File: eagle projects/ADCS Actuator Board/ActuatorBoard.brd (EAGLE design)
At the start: 91 x 91 mm, 155 parts, among them J19 TE_1-84953-1, J20 TE_1-84953-1, J21 TE_1-84953-1, J7 CNC_3221-10-0300-00, J8 CNC_3221-14-0300-00, U1 TVS991, U10 DRV10970_MOTOR_DRIVERDRV10970, U12 DRV10970_MOTOR_DRIVERDRV10970, U2 ADS7841E_2K5, U3 ADS7841E_2K5, U35 BD6210F-E2, U39 BD6210F-E2, U5 TVS991, U7 DRV10970_MOTOR_DRIVERDRV10970, U8 TVS991, U9 BD6210F-E2

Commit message: Staring REV B Act board
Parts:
- removed C119, C121, C122, C126, C129, C130, C139, C142, C25, C26: 0.1u, rcl:C0603
- removed C120, C140: 1u, rcl:C0603
- removed C123, C131: 0.1u, rcl:C0402
- removed C125, C141: 0.33u, rcl:C0603
- removed C127, C143: 2.2u, rcl:C0603
- removed C128, C144: 10u, rcl:C0603
- removed J19, J20, J21: TE_1-84953-1, my_library:TE_1-84953-1
- removed J5: (no value), my_library:1X03
- removed JP7, JP9: (no value), my_library:1X02
- removed JX, JY, JZ: (no value), my_library:2POL254
- removed R23: 100R, rcl:M0805
- removed R28, R29, R37, R38, R5: 1.8k, rcl:R0402
- removed R3, R4, R76: 5.1k, rcl:R0402
- removed R73, R74: 3.3k, rcl:R0603
- removed TP35, TP36, TP43, TP44, TP46, TP54, TP7: TESTPOINT, my_library:TP_P76H50
- removed U1: TVS991, my_library:SOT95P280X145-5N
- removed U35, U39, U9: BD6210F-E2, my_library:BD6221F-E2_SOIC8P127_500X620X171L30X42N
- added C1, C11, C2, C20, C34, C45, C50, C51, C54, C58, C63: 0.1u, rcl:C0603
- added C10, C3, C4, C46, C52, C6, C8: 0.1u, rcl:C0402
- added C12, C32, C55, C62: 1u, rcl:C0603
- added C19, C57: 0.33u, rcl:C0603
- added C28, C35, C59: 2.2u, rcl:C0603
- added C30, C36, C60: 10u, rcl:C0603
- added C31, C38, C61: 0.01u, rcl:C0603
- added C5, C7, C9: 1u, rcl:C0402
- added J11, J2: TE_1-84953-1, my_library:TE_1-84953-1
- added J12, J3: (no value), my_library:1X03
- added JP2, JP3: (no value), pinhead:1X02
- added R102, R103, R59, R60: 10K, rcl:R0603
- added R104, R61: 75K, rcl:R0603
- added R105, R106, R62, R63: 3.3k, rcl:R0603
- added R107, R108, R109, R64, R65, R66: 4.7k, rcl:R0402
- added R110, R111, R112, R113, R114, R115, R58, R67, R68, R69, R70, R71, R75: 5.1M, rcl:R0402
- added R116, R77: 10k, rcl:R0603
- added R117, R78: 2k, rcl:R0603
- added R118, R79: 1k, rcl:R0603
- added R119, R80: 100k, rcl:R0603
- added R47, R89: 0R, rcl:M0805
- added R57: 10K, rcl:R0402
- added R81: 5.1k, rcl:R0402
- added R82: 100R, rcl:M0805
- added R88: DNP, rcl:M0805
- added TP1, TP10, TP11, TP12, TP13, TP14, TP15, TP16, TP17, TP18, TP19, TP20, TP26, TP27, TP28, TP29, TP33, TP37, TP38, TP39, TP47, TP48, TP49, TP50, TP53, TP55, TP56, TP57, TP58, TP59, TP60, TP61, TP62, TP63, TP8, TP9: TESTPOINT, my_library:TP_P76H50
- added U11, U18: BD6210F-E2, my_library:BD6221F-E2_SOIC8P127_500X620X171L30X42N
- added U13, U17: LM2917MX/NOPB, my_library:SOIC14P127_865X600X175L83X41N_LM2917MX-NOPB
- added U16, U6: DRV10970_MOTOR_DRIVERDRV10970, my_library:SOP65P640X120-25T240X328N
- added U19: TSV991AILT, my_library:SOT95P280X145-5N
- added U4: ADS7841E_2K5, my_library:DBQ16
- C27: device rcl:C0402 -> rcl:C0603
- C41: value 2.2u -> 1u
- C42: value 10u -> 0.1u
- J4: value (none) -> TE_1-84953-1; device my_library:1X03 -> my_library:TE_1-84953-1
- JP5: device my_library:1X02 -> pinhead:1X02
- R1, R2: value 4.7k -> 10K; device rcl:R0402 -> rcl:R0603
- R11: value 4.7k -> 100R; device rcl:R0402 -> rcl:M0805
- R12: value 4.7k -> 5.1k
- R15: value 4.7k -> 1.8k
- R16: value 100R -> 1.8k; device rcl:M0805 -> rcl:R0402
- R17: value 5.1k -> 1.8k
- R19, R20: value 10K -> 4.7k; device rcl:R0603 -> rcl:R0402
- R21: value 75K -> 5.1M; device rcl:R0603 -> rcl:R0402
- R22: value 100R -> DNP
- R24: value 1.8k -> 0R; device rcl:R0402 -> rcl:M0805
- R25, R31: value 1.8k -> 5.1k
- R30: value 5.1k -> 100R; device rcl:R0402 -> rcl:M0805
- R35, R36: value 3.3k -> 5.1M; device rcl:R0603 -> rcl:R0402
- R41: value 5.1M -> 1.8k
- R42: value 5.1M -> DNP; device rcl:R0402 -> rcl:M0805
- R44: value 5.1M -> 10k; device rcl:R0402 -> rcl:R0603
- R48: value 10K -> 2k
- R49: value 10K -> 1k
- R7: value 4.7k -> 75K; device rcl:R0402 -> rcl:R0603
- R72: value 75K -> 100k
- R8, R9: value 4.7k -> 3.3k; device rcl:R0402 -> rcl:R0603
- R83: value 10K -> 5.1k; device rcl:R0603 -> rcl:R0402
- R84: value 10K -> 1.8k; device rcl:R0603 -> rcl:R0402
- R85: value 75K -> 1.8k; device rcl:R0603 -> rcl:R0402
- R86, R87: value 3.3k -> 1.8k; device rcl:R0603 -> rcl:R0402
- U10: value DRV10970_MOTOR_DRIVERDRV10970 -> LM2917MX/NOPB; device my_library:SOP65P640X120-25T240X328N -> my_library:SOIC14P127_865X600X175L83X41N_LM2917MX-NOPB
- U12: value DRV10970_MOTOR_DRIVERDRV10970 -> TSV991AILT; device my_library:SOP65P640X120-25T240X328N -> my_library:SOT95P280X145-5N
- U5: value TVS991 -> BD6210F-E2; device my_library:SOT95P280X145-5N -> my_library:BD6221F-E2_SOIC8P127_500X620X171L30X42N
- U8: value TVS991 -> TSV991AILT
- moved R45 169.7 mm to (107.3, 94.0)
- moved R46 169.7 mm to (112.4, 94.0)
- moved R41 158.8 mm to (11.4, 67.9), flipped to the bottom, turned to 270 degrees
- moved R42 151.7 mm to (18.4, 61.0), flipped to the bottom
- moved R34 149.3 mm to (12.7, 67.9), flipped to the bottom
- moved R44 145.8 mm to (34.3, 57.1), turned to 0 degrees
- moved R32 145.0 mm to (11.4, 65.7), flipped to the bottom, turned to 270 degrees
- moved R33 141.3 mm to (11.4, 60.6), flipped to the bottom, turned to 270 degrees
- moved R31 140.7 mm to (12.1, 62.5), flipped to the bottom, turned to 180 degrees
- moved R25 139.9 mm to (12.1, 63.8), flipped to the bottom, turned to 180 degrees
- moved R43 136.8 mm to (41.3, 52.4), flipped to the bottom, turned to 270 degrees
- moved R40 131.8 mm to (42.5, 52.4), flipped to the bottom, turned to 270 degrees
- moved R39 131.5 mm to (38.7, 52.4), flipped to the bottom, turned to 270 degrees
- moved R6 129.6 mm to (12.1, 51.1), flipped to the bottom, turned to 180 degrees
- moved R24 128.3 mm to (18.4, 52.7), flipped to the bottom
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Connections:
- removed net MAG_CUR_SEN_Y: R22.2, R30.2, U35.1
- removed net MAG_CUR_SEN_Z: R16.2, R17.2, U39.1
- removed net MAG_Y_FIN: TP43.1, U35.4
- removed net N$10: R28.2, R76.1, U1.3
- removed net N$105: C139.1, U12.9
- removed net N$106: C140.2, U12.8
- removed net N$107: C139.2, U12.10
- removed net N$108: C143.1, U12.16
- removed net N$109: C141.1, U12.22
- removed net N$18: R28.1, R37.1, R38.2
- removed net N$19 (its old number): R40.2, U10.1
- removed net N$23 (its old number): R43.1, U10.20
- removed net N$3 (its old number): R39.2, U7.1
- removed net N$33: JP7.2, U35.7
- removed net N$4: R5.1, R6.1, U8.4
- removed net N$67: JP9.2, U39.7
- removed net N$7: R29.1, R4.1, U1.4
- removed net N$87: C119.1, U10.9
- removed net N$88: C120.2, U10.8
- removed net N$89: C119.2, U10.10
- removed net N$90: C127.1, U10.16
- removed net N$91: C125.1, U10.22
- removed net OUT1_Y: JY.1, R22.1, R3.2
- removed net OUT1_Z: JZ.1, R16.1, R23.1, R4.2, R6.2
- removed net OUT2_Y: JP7.1, JY.2
- removed net OUT2_Z: JP9.1, JZ.2
- new net !CS!_SPD_SENSE_RW: J7.1, U4.15
- new net N$28: R21.2, U7.1
- new net N$29: R35.1, U7.20
- new net N$30: C41.2, R72.2, TP13.1, U10.3, U10.4
- new net N$31: R48.1, R49.2, U10.11
- new net N$32: C8.1, R57.1, U4.7
- new net N$34: TP1.1, U4.5
- new net N$35: R58.2, U4.13
- new net N$36: C11.1, U6.9
- new net N$38: C12.2, U6.8
- new net N$39: C11.2, U6.10
- new net N$40: C28.1, U6.16
- new net N$41: C19.1, U6.22
- new net N$43: R67.2, U6.1
- new net N$44: R68.1, U6.20
- new net N$49: C32.2, R80.2, TP28.1, U13.3, U13.4
- new net N$50: R78.1, R79.2, U13.11
- new net N$51: C31.2, U13.2
- new net N$52: C38.2, U10.2
- new net N$53: R81.1, R84.2, U19.3
- new net N$54: R84.1, R86.1, R87.2
- new net N$55: R82.2, R88.2, R89.1
- new net N$63: C54.1, U16.9
- new net N$64: C55.2, U16.8
- new net N$65: C54.2, U16.10
- new net N$66: C59.1, U16.16
- new net N$68: C57.1, U16.22
- new net N$69: R110.2, U16.1
- new net N$70: R111.1, U16.20
- new net N$72: R117.1, R118.2, U17.11
- new net N$73: C61.2, U17.2
- new net RW_X_SPD: R44.2, TP12.1, U10.10, U10.5, U4.3
- new net RW_Y_SPD: R116.2, TP56.1, U17.10, U17.5, U4.2
- new net RW_Z_SPD: R77.2, TP27.1, U13.10, U13.5, U4.4
- new net X_DNC_1: R36.1, U10.6
- new net X_DNC_2: R39.1, U10.7
- new net X_DNC_3: R43.1, U10.14
- new net X_DNC_4: R40.1, U10.13
- new net Y_DNC_1: R112.1, U17.6
- new net Y_DNC_2: R113.1, U17.7
- new net Y_DNC_3: R115.1, U17.14
- new net Y_DNC_4: R114.1, U17.13
- new net Z_DNC_1: R69.1, U13.6
- new net Z_DNC_2: R70.1, U13.7
- new net Z_DNC_3: R75.1, U13.14
- new net Z_DNC_4: R71.1, U13.13
- net +3V3: now also C10.1, C34.2, C4.1, C42.2, C5.1, C6.1, C63.2, C7.1, C9.1, R105.1, R106.1, R118.1, R17.2, R34.2, R49.1, R57.2, R62.1, R63.1, R79.1, R8.1, R86.2, R9.1, U10.8, U10.9, U13.8, U13.9, U17.8, U17.9, U4.1, U4.8, U4.9; no longer R31.2, R33.2, R35.1, R36.1, R37.2, R73.1, R74.1, R86.1, R87.1
- net +5V: now also C1.1, C12.1, C2.2, C3.1, C30.1, C36.1, C45.2, C46.1, C50.1, C51.2, C52.1, C55.1, C60.1, J11.1, J12.3, J2.1, J3.3, J4.1, R102.2, R107.2, R108.2, R109.2, R20.2, R59.2, R64.2, R65.2, R66.2, U11.2, U11.3, U11.6, U12.5, U16.15, U18.2, U18.3, U18.6, U19.5, U5.2, U5.3, U5.6, U6.15; no longer C120.1, C121.1, C122.2, C123.1, C128.1, C129.1, C130.2, C131.1, C140.1, C144.1, C25.1, C26.2, C42.1, J19.1, J20.1, J21.1, J4.3, J5.3, R11.2, R12.2, R15.2, R2.2, R48.2, R7.2, R8.2, R83.2, R9.2, U1.5, U10.15, U12.15, U35.2, U35.3, U35.6, U39.2, U39.3, U39.6, U5.5, U9.2, U9.3, U9.6
- net BRKMOD_X: now also J6.2, U7.21; no longer J4.2, U10.21
- net BRKMOD_Y: now also J12.2, U16.21; no longer J6.2, U7.21
- net BRKMOD_Z: now also J3.2, U6.21; no longer J5.2, U12.21
- net CUR_OUT1: no longer R5.2, U8.1
- net CUR_OUT2: no longer R24.2, TP46.1, U5.1
- net CUR_OUT3: now also R16.2, R33.2, R85.2, TP10.1, TP30.1, TP51.1, U12.1, U19.1, U8.1; no longer R29.2, TP54.1, U1.1
- net GND: now also C1.2, C10.2, C19.2, C2.1, C20.2, C28.2, C3.2, C30.2, C31.1, C32.1, C34.1, C35.2, C36.2, C38.1, C4.2, C41.1, C42.1, C45.1, C46.2, C5.2, C50.2, C51.1, C52.2, C57.2, C58.2, C59.2, C6.2, C60.2, C61.1, C62.1, C63.1, C7.2, C8.2, C9.2, J11.5, J11.TAB1, J11.TAB2, J12.1, J2.5, J2.TAB1, J2.TAB2, J3.1, J4.5, J4.TAB1, J4.TAB2, R103.1, R104.1, R110.1, R111.2, R112.2, R113.2, R114.2, R115.2, R116.1, R117.2, R119.1, R18.1, R2.1, R35.2, R36.2, R39.2, R40.2, R44.1, R48.2, R58.1, R60.1, R61.1, R67.1, R68.2, R69.2, R7.1, R70.2, R71.2, R75.2, R77.1, R78.2, R80.1, R87.1, U11.8, U12.2, U13.12, U16.12, U16.25, U17.12, U18.8, U19.2, U4.10, U4.11, U4.6, U5.8, U6.12, U6.25; no longer C121.2, C122.1, C123.2, C125.2, C126.2, C127.2, C128.2, C129.2, C130.1, C131.2, C141.2, C142.2, C143.2, C144.2, C25.2, C26.1, C41.2, C42.2, J19.5, J19.TAB1, J19.TAB2, J20.5, J20.TAB1, J20.TAB2, J21.5, J21.TAB1, J21.TAB2, J4.1, J5.1, R20.1, R32.1, R34.1, R38.1, R39.1, R40.1, R42.2, R44.2, R49.1, R84.1, R85.1, U1.2, U10.25, U12.12, U12.25, U35.8, U39.8, U5.2, U9.8
- net MAG_CUR_SEN_X: now also R24.2, R25.2, R47.2, R6.2, R81.2, R89.2, TP17.1, TP34.1, TP52.1, U11.1, U18.1, U5.1; no longer R23.2, R76.2, U9.1
- net MAG_X_FIN: now also TP24.1, TP47.1, TP8.1, U11.4, U18.4, U5.4; no longer TP35.1, U9.4
- net MAG_X_RIN: now also TP25.1, TP48.1, TP9.1, U11.5, U18.5, U5.5; no longer TP36.1, U9.5
- net MAG_Y_RIN: no longer TP44.1, U35.5
- net MAG_Z_FIN: no longer TP51.1, U39.4
- net MAG_Z_RIN: no longer TP52.1, U39.5
- net N$16: now also R11.2, R22.2, R24.1; no longer JP5.2, U9.7
- net N$17: now also R31.1, U12.4; no longer R34.2
- net N$20: now also R25.1, R32.2, U12.3; no longer R41.2, U12.1
- net N$21: now also R32.1, R34.1, R41.2; no longer R18.1, R31.1, R32.2
- net N$22: now also R30.2, R42.2, R47.1; no longer R42.1, U12.20
- net N$24: now also C35.1, U7.16; no longer R44.1, U7.20
- net N$48: now also R83.1, R85.1, U19.4; no longer R25.1
- net N$6: now also R12.1, R16.1, U8.4; no longer R24.1, R3.1, U5.4
- net N$71: now also C62.2, R119.2, TP57.1, U17.3, U17.4; no longer C41.1, U7.16
- net N$8: now also R15.2, R6.1; no longer R17.1, R18.2
- net N$9: now also R15.1, R17.1, R18.2; no longer R25.2, R30.1, U5.3
- net OUT1_X: now also JP2.1, JP3.1, JP5.1, R11.1, R12.2, R22.1, R30.1, R31.2, R42.1, R82.1, R83.2, R88.1, TP21.1, TP39.1, TP62.1; no longer JX.1
- net OUT2_X: now also JP2.2, JP3.2, JP5.2, TP22.1, TP40.1, TP63.1, U11.7, U18.7, U5.7; no longer JP5.1, JX.2
- net RW_X_DIR: now also U7.23; no longer U10.23
- net RW_X_I_SENS: now also R7.2, TP11.1, U7.17; no longer R72.2, TP34.1, U10.17
- net RW_X_LOCK: now also R9.2, U7.18; no longer R74.2, U10.18
- net RW_X_OUTFG: now also R8.2, TP23.1, U10.1, U7.24; no longer J8.13, R73.2, U10.24
- net RW_X_SPEED_CTRL: now also U7.19; no longer U10.19
- net RW_Y_DIR: now also U16.23; no longer U7.23
- net RW_Y_I_SENS: now also R104.2, TP55.1, U16.17; no longer R21.2, TP30.1, U7.17
- net RW_Y_LOCK: now also R106.2, U16.18; no longer R36.2, U7.18
- net RW_Y_OUTFG: now also R105.2, TP61.1, U16.24, U17.1; no longer J7.1, R35.2, U7.24
- net RW_Y_SPEED_CTRL: now also U16.19; no longer U7.19
- net RW_Z_DIR: now also U6.23; no longer U12.23
- net RW_Z_I_SENS: now also R61.2, TP26.1, U6.17; no longer R85.2, TP40.1, U12.17
- net RW_Z_LOCK: now also R63.2, U6.18; no longer R87.2, U12.18
- net RW_Z_OUTFG: now also R62.2, TP38.1, U13.1, U6.24; no longer J7.2, R86.2, U12.24
- net RW_Z_SPEED_CTRL: now also U6.19; no longer U12.19
- net UCB0_SPI_CLK: now also U4.16
- net UCB0_SPI_MISO: now also U4.12
- net UCB0_SPI_MOSI: now also U4.14
- net VINT/2_X: now also C16.1, R1.1, R2.2, U7.3, U7.5, U7.7; no longer C126.1, R48.1, R49.2, U10.3, U10.5, U10.7
- net VINT/2_Y: now also C58.1, R102.1, R103.2, U16.3, U16.5, U16.7; no longer C16.1, R19.1, R20.2, U7.3, U7.5, U7.7
- net VINT/2_Z: now also C20.1, R59.1, R60.2, U6.3, U6.5, U6.7; no longer C142.1, R83.1, R84.2, U12.3, U12.5, U12.7
- net X_HALL_A: now also J4.3, R19.1, U7.2; no longer J19.3, R2.1, U10.2
- net X_HALL_B: now also J4.4, R10.1, U7.4; no longer J19.4, R1.1, U10.4
- net X_HALL_C: now also J4.2, R20.1, U7.6; no longer J19.2, R7.1, U10.6
- net X_PHASE_A: now also J4.10, J4.11, TP14.1, U7.14; no longer J19.10, J19.11, U10.14
- net X_PHASE_B: now also J4.8, J4.9, TP15.1, U7.13; no longer J19.8, J19.9, U10.13
- net X_PHASE_C: now also U7.11; no longer J19.6, J19.7, U10.11
- net Y_HALL_A: now also J11.3, R108.1, TP53.1, U16.2; no longer J20.3, R9.1, TP25.1, U7.2
- net Y_HALL_B: now also J11.4, R107.1, TP50.1, U16.4; no longer J20.4, R8.1, TP24.1, U7.4
- net Y_HALL_C: now also J11.2, R109.1, TP49.1, U16.6; no longer J20.2, R10.1, TP23.1, U7.6
- net Y_PHASE_A: now also J11.10, J11.11, TP58.1, U16.14; no longer J20.10, J20.11, U7.14
- net Y_PHASE_B: now also J11.8, J11.9, TP59.1, U16.13; no longer J20.8, J20.9, U7.13
- net Y_PHASE_C: now also J11.6, J11.7, TP60.1, U16.11; no longer J20.6, J20.7, U7.11
- net Z_HALL_A: now also J2.3, R65.1, TP20.1, U6.2; no longer J21.3, R12.1, TP22.1, U12.2
- net Z_HALL_B: now also J2.4, R64.1, TP19.1, U6.4; no longer J21.4, R11.1, TP21.1, U12.4
- net Z_HALL_C: now also J2.2, R66.1, TP18.1, U6.6; no longer J21.2, R15.1, TP7.1, U12.6
- net Z_PHASE_A: now also J2.10, J2.11, TP29.1, U6.14; no longer J21.10, J21.11, U12.14
- net Z_PHASE_B: now also J2.8, J2.9, TP33.1, U6.13; no longer J21.8, J21.9, U12.13
- net Z_PHASE_C: now also J2.6, J2.7, J4.6, J4.7, TP16.1, TP37.1, U6.11; no longer J21.6, J21.7, U12.11
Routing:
- net RW_Y_SPEED_CTRL: track 105.1 -> 7.73 mm, vias 5 -> 0
- net RW_X_DIR: track 91.8 -> 5.49 mm, vias 5 -> 1
- net MAG_Z_RIN: track 84.2 -> 0.00 mm
- net RW_Y_OUTFG: track 100.9 -> 17.1 mm
- net MAG_Y_RIN: track 79.2 -> 0.00 mm
- net MAG_Z_FIN: track 78.1 -> 0.00 mm, vias 1 -> 0
- net RW_Y_DIR: track 82.8 -> 5.49 mm, vias 4 -> 1
- net RW_X_SPEED_CTRL: track 84.5 -> 7.73 mm, vias 3 -> 0
- net RW_X_OUTFG: track 93.6 -> 19.4 mm
- net MAG_X_RIN: track 76.1 -> 5.77 mm, vias 1 -> 0
- net MAG_X_FIN: track 69.1 -> 5.77 mm
- net !CS!_CURR_SENSE_MTQR: track 61.2 -> 0.00 mm, vias 1 -> 0
- net UCB0_SPI_CLK: track 61.1 -> 0.00 mm, vias 2 -> 0
- net UCB0_SPI_MISO: track 56.6 -> 0.00 mm, vias 1 -> 0
- net !CS!_CURR_SENSE_RW: track 50.0 -> 0.00 mm, vias 3 -> 0
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- removed copper zone on layer 15, net +5V
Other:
- board text added: "ACTUATOR BOARD - REV B"
- board text removed: "ACTUATOR BOARD - REV A"

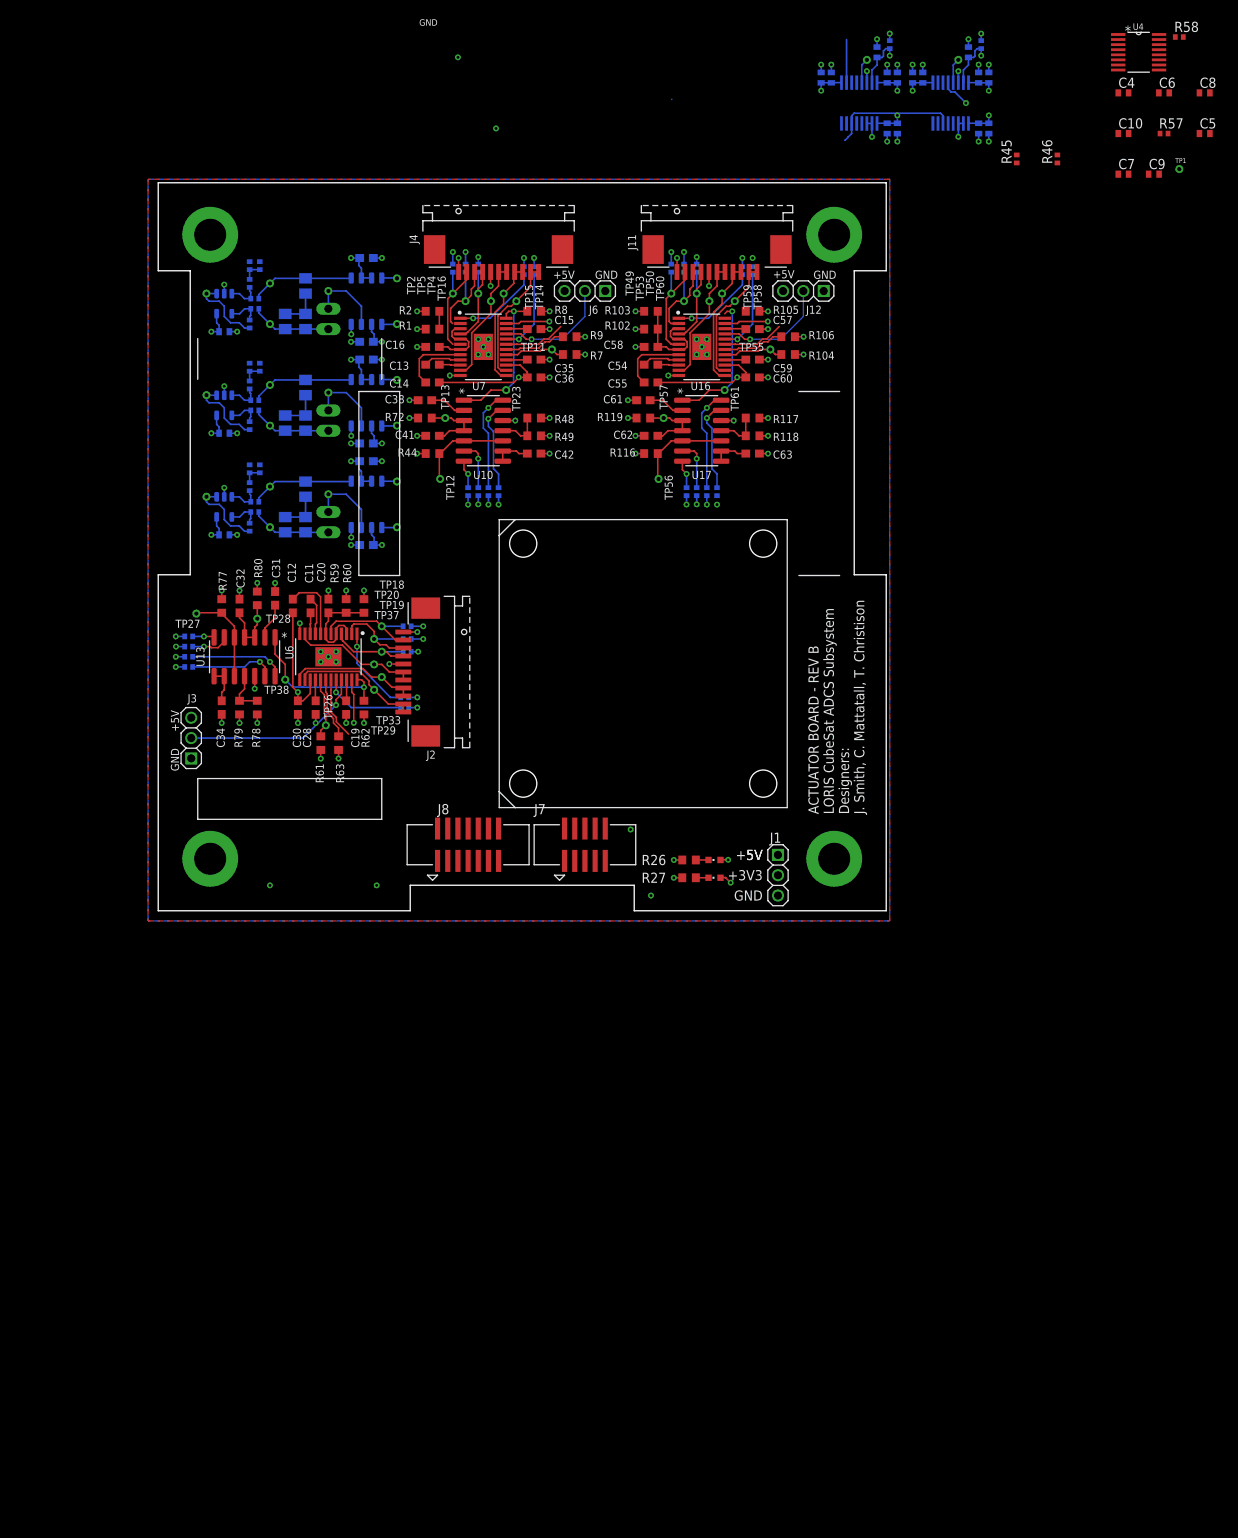
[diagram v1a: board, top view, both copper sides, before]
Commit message: Added FV converters, replaced connectors
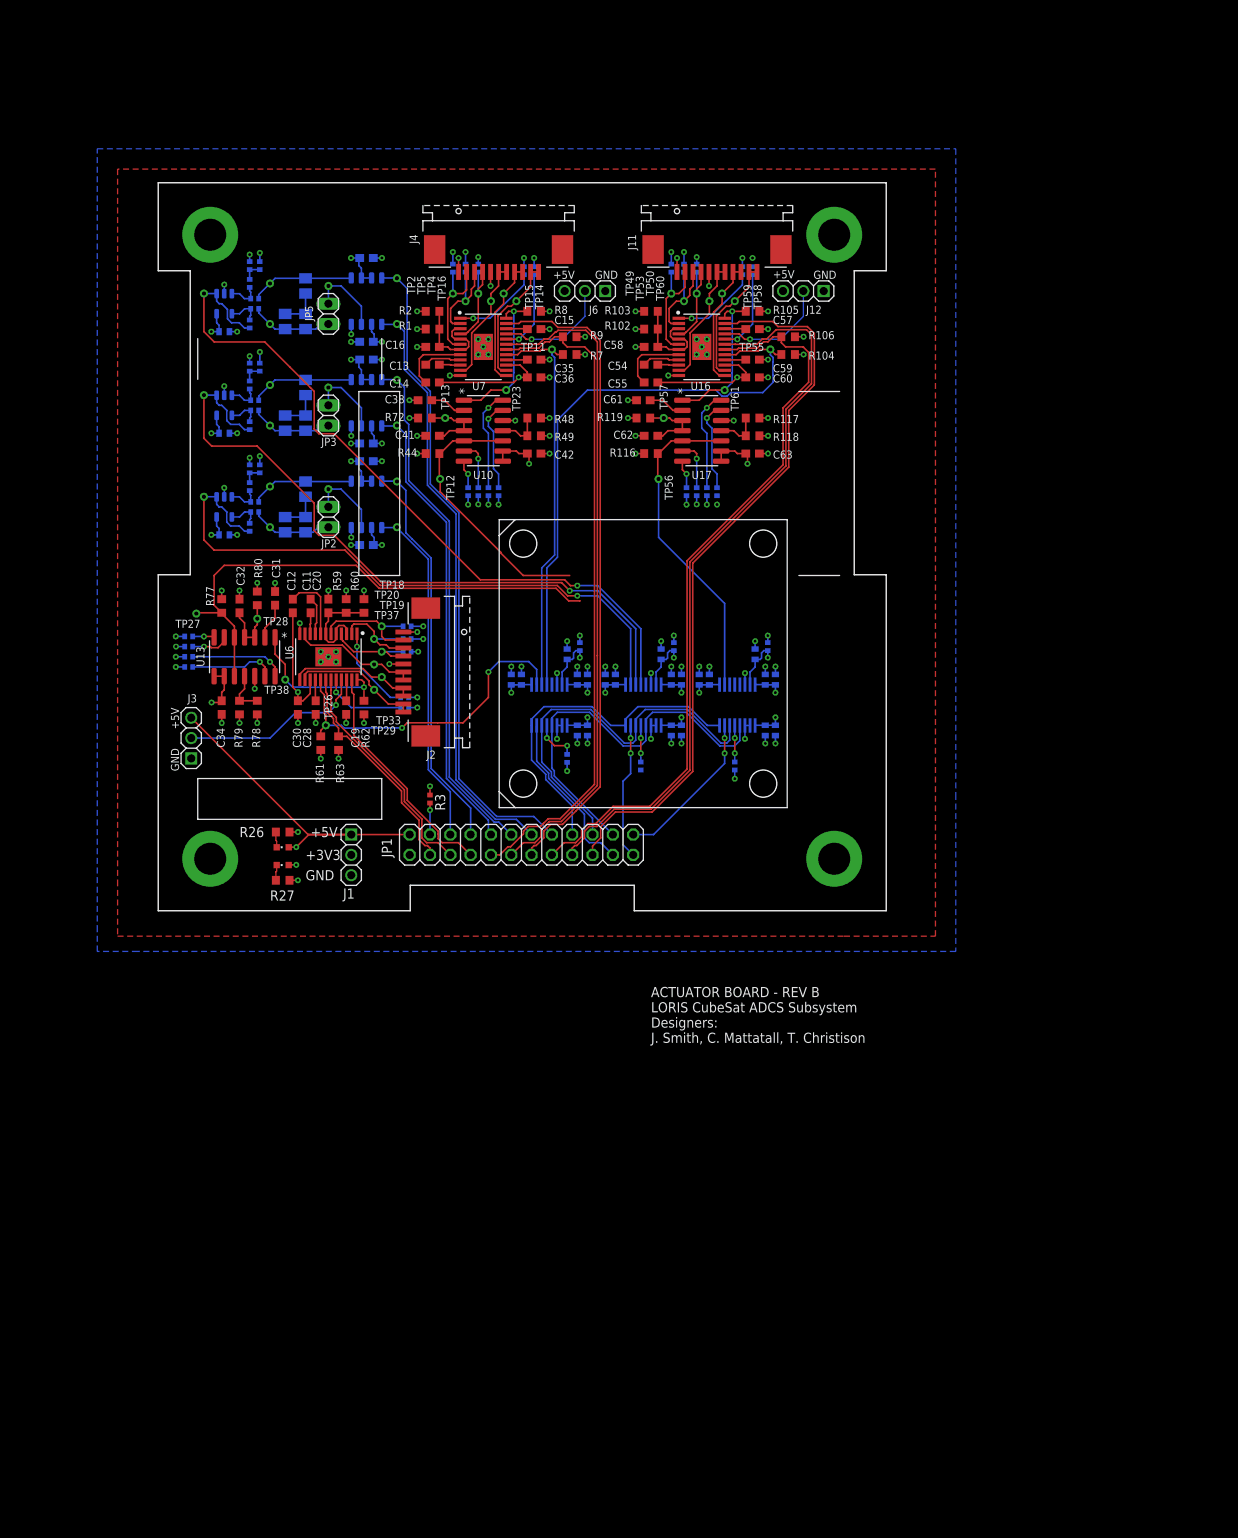
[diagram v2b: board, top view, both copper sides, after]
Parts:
- removed C10, C17, C21, C23, C29, C37, C39, C4, C43, C56, C6, C8: 0.1u, rcl:C0402
- removed C18, C22, C24, C33, C40, C44, C5, C7, C9: 1u, rcl:C0402
- removed J7: CNC_3221-10-0300-00, my_library:CNC_3221-10-0300-00
- removed J8: CNC_3221-14-0300-00, my_library:CNC_3221-14-0300-00
- removed R13, R14, R57: 10K, rcl:R0402
- removed R45, R46, R58: 5.1M, rcl:R0402
- removed TP1, TP31, TP32: TESTPOINT, my_library:TP_P76H50
- removed U2, U3, U4: ADS7841E_2K5, my_library:DBQ16
- added C65, C67, C69, C71, C72, C74, C76, C78, C86, C88, C90, C92: 0.1u, rcl:C0402
- added C66, C68, C70, C73, C75, C77, C87, C89, C91: 1u, rcl:C0402
- added JP1: (no value), pinhead:2X12
- added R23, R3, R37, R51: 5.1M, rcl:R0402
- added R29, R5, R50: 10K, rcl:R0402
- added U14, U20, U9: ADS7841E_2K5, my_library:DBQ16
- R17, R34, R86: value 1.8k -> 2.2k
- R18, R41, R87: value 1.8k -> 1.1k
- moved LED1 54.0 mm to (15.6, 7.94)
- moved LED2 54.0 mm to (15.6, 5.71)
- moved J1 53.4 mm to (24.1, 6.99)
- moved R26 50.9 mm to (15.6, 9.84), turned to 180 degrees
- moved R27 50.8 mm to (15.6, 3.81), turned to 180 degrees
- moved TP40 0.64 mm to (21.3, 65.4)
- moved TP63 0.64 mm to (21.3, 78.1)
- moved JP2 0.63 mm to (21.3, 49.2), flipped to the top
- moved JP3 0.63 mm to (21.3, 61.9), flipped to the top
- moved TP22 0.63 mm to (21.3, 52.7)
- moved JP5 0.63 mm to (21.3, 74.6), flipped to the top
- moved TP10 0.32 mm to (5.71, 51.8)
- moved TP30 0.32 mm to (5.71, 64.5)
- moved TP51 0.32 mm to (5.71, 77.2)
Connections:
- removed net MAG_Y_FIN\: J8.6
- removed net N$11: C23.1, R14.1, U3.7
- removed net N$12: TP32.1, U3.5
- removed net N$13: C43.1, R13.1, U2.7
- removed net N$15: TP31.1, U2.5
- removed net N$2: R46.2, U3.13
- removed net N$32: C8.1, R57.1, U4.7
- removed net N$34: TP1.1, U4.5
- removed net N$35: R58.2, U4.13
- removed net N$37: J7.10
- removed net N$42: J7.9
- new net MAG_CUR_SEN_Y: R25.2, R47.2, TP34.1, U11.1
- new net MAG_CUR_SEN_Z: R81.2, R89.2, TP52.1, U18.1
- new net MAG_Y_FIN: JP1.12, TP24.1, U11.4
- new net N$18: C69.1, R5.1, U9.7
- new net N$25: R23.2, U9.13
- new net N$26: U9.5
- new net N$33: C76.1, R29.1, U14.7
- new net N$45: R37.2, U14.13
- new net N$46: U14.5
- new net N$58: C90.1, R50.1, U20.7
- new net N$59: R51.2, U20.13
- new net N$60: U20.5
- new net OUT1_Y: JP3.1, R30.1, R31.2, R42.1, TP39.1
- new net OUT1_Z: JP5.1, R82.1, R83.2, R88.1, TP62.1
- new net OUT2_Y: JP3.2, TP40.1, U11.7
- new net OUT2_Z: JP5.2, TP63.1, U18.7
- net !CS!_CURR_SENSE_MTQR: now also JP1.23, U9.15; no longer J7.5, U2.15
- net !CS!_CURR_SENSE_RW: now also JP1.21, U14.15; no longer J7.3, U3.15
- net !CS!_SPD_SENSE_RW: now also JP1.24, U20.15; no longer J7.1, U4.15
- net +3V3: now also C65.1, C66.1, C67.1, C68.1, C70.1, C71.1, C72.1, C73.1, C74.1, C75.1, C77.1, C78.1, C86.1, C87.1, C88.1, C89.1, C91.1, C92.1, JP1.1, R29.2, R5.2, R50.2, U14.1, U14.8, U14.9, U20.1, U20.8, U20.9, U9.1, U9.8, U9.9; no longer C10.1, C17.1, C18.1, C21.1, C22.1, C24.1, C29.1, C33.1, C37.1, C39.1, C4.1, C40.1, C44.1, C5.1, C56.1, C6.1, C7.1, C9.1, J7.7, R13.2, R14.2, R17.2, R34.2, R57.2, R86.2, U2.1, U2.8, U2.9, U3.1, U3.8, U3.9, U4.1, U4.8, U4.9
- net +5V: now also JP1.2, R17.2, R34.2, R86.2; no longer J8.14
- net CUR_OUT1: now also R16.2, TP10.1, U8.1, U9.2; no longer U2.2
- net CUR_OUT2: now also R33.2, TP30.1, U12.1, U9.3; no longer U2.3
- net CUR_OUT3: now also U9.4; no longer R16.2, R33.2, TP10.1, TP30.1, U12.1, U2.4, U8.1
- net GND: now also C65.2, C66.2, C67.2, C68.2, C69.2, C70.2, C71.2, C72.2, C73.2, C74.2, C75.2, C76.2, C77.2, C78.2, C86.2, C87.2, C88.2, C89.2, C90.2, C91.2, C92.2, R23.1, R3.1, R37.1, R51.1, U14.10, U14.11, U14.6, U20.10, U20.11, U20.6, U9.10, U9.11, U9.6; no longer C10.2, C17.2, C18.2, C21.2, C22.2, C23.2, C24.2, C29.2, C33.2, C37.2, C39.2, C4.2, C40.2, C43.2, C44.2, C5.2, C56.2, C6.2, C7.2, C8.2, C9.2, R45.2, R46.1, R58.1, U2.10, U2.11, U2.6, U3.10, U3.11, U3.6, U4.10, U4.11, U4.6
- net MAG_CUR_SEN_X: no longer R25.2, R47.2, R81.2, R89.2, TP34.1, TP52.1, U11.1, U18.1
- net MAG_X_FIN: now also JP1.8; no longer J8.10, TP24.1, TP47.1, U11.4, U18.4
- net MAG_X_RIN: now also JP1.6; no longer J8.12, TP25.1, TP48.1, U11.5, U18.5
- net MAG_Y_RIN: now also JP1.10, TP25.1, U11.5; no longer J8.8
- net MAG_Z_FIN: now also JP1.16, TP47.1, U18.4; no longer J8.2
- net MAG_Z_RIN: now also JP1.14, TP48.1, U18.5; no longer J8.4
- net N$1: now also JP1.4, R3.2; no longer R45.1, U2.13
- net OUT1_X: no longer JP3.1, JP5.1, R30.1, R31.2, R42.1, R82.1, R83.2, R88.1, TP39.1, TP62.1
- net OUT2_X: no longer JP3.2, JP5.2, TP40.1, TP63.1, U11.7, U18.7
- net RW_X_DIR: now also JP1.13; no longer J8.7
- net RW_X_I_SENS: now also U14.3; no longer U3.3
- net RW_X_LOCK: now also JP1.9
- net RW_X_SPD: now also U20.3; no longer U4.3
- net RW_X_SPEED_CTRL: now also JP1.11; no longer J8.1
- net RW_Y_DIR: now also JP1.19; no longer J8.9
- net RW_Y_I_SENS: now also U14.4; no longer U3.2
- net RW_Y_LOCK: now also JP1.15
- net RW_Y_SPD: now also U20.2; no longer U4.2
- net RW_Y_SPEED_CTRL: now also JP1.17; no longer J8.3
- net RW_Z_DIR: now also JP1.7; no longer J8.11
- net RW_Z_I_SENS: now also U14.2; no longer U3.4
- net RW_Z_LOCK: now also JP1.3
- net RW_Z_SPD: now also U20.4; no longer U4.4
- net RW_Z_SPEED_CTRL: now also JP1.5; no longer J8.5
- net UCB0_SPI_CLK: now also JP1.18, U14.16, U20.16, U9.16; no longer J7.4, U2.16, U3.16, U4.16
- net UCB0_SPI_MISO: now also JP1.22, U14.12, U20.12, U9.12; no longer J7.6, U2.12, U3.12, U4.12
- net UCB0_SPI_MOSI: now also JP1.20, U14.14, U20.14, U9.14; no longer J7.8, U2.14, U3.14, U4.14
- net X_PHASE_C: now also J4.6, J4.7, TP16.1
- net Z_PHASE_C: no longer J4.6, J4.7, TP16.1
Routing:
- net CUR_OUT2: track 0.00 -> 87.0 mm, vias 0 -> 1
- net RW_Y_DIR: track 5.49 -> 91.3 mm, vias 1 -> 0
- net RW_Y_SPEED_CTRL: track 7.73 -> 92.7 mm
- net RW_Y_LOCK: track 7.73 -> 92.6 mm
- net MAG_Z_FIN: track 0.00 -> 82.2 mm
- net RW_X_DIR: track 5.49 -> 81.7 mm, vias 1 -> 0
- net RW_X_LOCK: track 7.73 -> 83.4 mm
- net RW_X_SPEED_CTRL: track 7.73 -> 83.0 mm
- net MAG_Z_RIN: track 0.00 -> 74.2 mm
- net CUR_OUT1: track 5.38 -> 79.1 mm, vias 0 -> 1
- net RW_Y_I_SENS: track 7.61 -> 75.0 mm
- net MAG_Y_FIN: track 0.00 -> 65.0 mm
- net CUR_OUT3: track 28.7 -> 93.2 mm, vias 0 -> 1
- net MAG_Y_RIN: track 0.00 -> 57.9 mm
- net RW_Z_SPD: track 11.8 -> 64.9 mm
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- added copper zone on layer 15, net +5V
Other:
- board text removed: "5V"
